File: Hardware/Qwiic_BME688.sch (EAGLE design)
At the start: 28 parts, among them J1 DNP, J2 QWIIC_RA, J4 QWIIC_RA, U1 BME688LGA

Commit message: Board routed
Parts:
- C1, C2: device SparkFun-Capacitors:0.1UF-0402-16V-10% -> SparkFun-Capacitors:0.1UF-0603-100V-10%
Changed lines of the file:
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@@
 <grid distance="0.1" unitdist="inch" unit="inch" style="lines" multiple="1" display="no" altdistance="0.01" altunitdist="inch" altunit="inch"/>
 <layers>
-<layer number="1" name="Top" color="4" fill="1" visible="no" active="no"/>
-<layer number="2" name="Route2" color="1" fill="3" visible="no" active="no"/>
-<layer number="3" name="Route3" color="4" fill="3" visible="no" active="no"/>
-<layer number="4" name="Route4" color="1" fill="4" visible="no" active="no"/>
-<layer number="5" name="Route5" color="4" fill="4" visible="no" active="no"/>
-<layer number="6" name="Route6" color="1" fill="8" visible="no" active="no"/>
-<layer number="7" name="Route7" color="4" fill="8" visible="no" active="no"/>
-<layer number="8" name="Route8" color="1" fill="2" visible="no" active="no"/>
-<layer number="9" name="Route9" color="4" fill="2" visible="no" active="no"/>
-<layer number="10" name="Route10" color="1" fill="7" visible="no" active="no"/>
-<layer number="11" name="Route11" color="4" fill="7" visible="no" active="no"/>
-<layer number="12" name="Route12" color="1" fill="5" visible="no" active="no"/>
-<layer number="13" name="Route13" color="4" fill="5" visible="no" active="no"/>
-<layer number="14" name="Route14" color="1" fill="6" visible="no" active="no"/>
-<layer number="15" name="Route15" color="4" fill="6" visible="no" active="no"/>
-<layer number="16" name="Bottom" color="1" fill="1" visible="no" active="no"/>
-<layer number="17" name="Pads" color="2" fill="1" visible="no" active="no"/>
-<layer number="18" name="Vias" color="2" fill="1" visible="no" active="no"/>
-<layer number="19" name="Unrouted" color="6" fill="1" visible="no" active="no"/>
-<layer number="20" name="Dimension" color="24" fill="1" visible="no" active="no"/>
-<layer number="21" name="tPlace" color="16" fill="1" visible="no" active="no"/>
-<layer number="22" name="bPlace" color="14" fill="1" visible="no" active="no"/>
-<layer number="23" name="tOrigins" color="15" fill="1" visible="no" active="no"/>
-<layer number="24" name="bOrigins" color="15" fill="1" visible="no" active="no"/>
-<layer number="25" name="tNames" color="7" fill="1" visible="no" active="no"/>
-<layer number="26" name="bNames" color="7" fill="1" visible="no" active="no"/>
-<layer number="27" name="tValues" color="7" fill="1" visible="no" active="no"/>
-<layer number="28" name="bValues" color="7" fill="1" visible="no" active="no"/>
+<layer number="1" name="Top" color="4" fill="1" visible="yes" active="no"/>
+<layer number="2" name="Route2" color="1" fill="3" visible="yes" active="no"/>
+<layer number="3" name="Route3" color="4" fill="3" visible="yes" active="no"/>
+<layer number="4" name="Route4" color="1" fill="4" visible="yes" active="no"/>
+<layer number="5" name="Route5" color="4" fill="4" visible="yes" active="no"/>
+<layer number="6" name="Route6" color="1" fill="8" visible="yes" active="no"/>
+<layer number="7" name="Route7" color="4" fill="8" visible="yes" active="no"/>
+<layer number="8" name="Route8" color="1" fill="2" visible="yes" active="no"/>
+<layer number="9" name="Route9" color="4" fill="2" visible="yes" active="no"/>
+<layer number="10" name="Route10" color="1" fill="7" visible="yes" active="no"/>
+<layer number="11" name="Route11" color="4" fill="7" visible="yes" active="no"/>
+<layer number="12" name="Route12" color="1" fill="5" visible="yes" active="no"/>
+<layer number="13" name="Route13" color="4" fill="5" visible="yes" active="no"/>
+<layer number="14" name="Route14" color="1" fill="6" visible="yes" active="no"/>
+<layer number="15" name="Route15" color="4" fill="6" visible="yes" active="no"/>
+<layer number="16" name="Bottom" color="1" fill="1" visible="yes" active="no"/>
+<layer number="17" name="Pads" color="2" fill="1" visible="yes" active="no"/>
+<layer number="18" name="Vias" color="2" fill="1" visible="yes" active="no"/>
+<layer number="19" name="Unrouted" color="6" fill="1" visible="yes" active="no"/>
+<layer number="20" name="Dimension" color="24" fill="1" visible="yes" active="no"/>
+<layer number="21" name="tPlace" color="16" fill="1" visible="yes" active="no"/>
+<layer number="22" name="bPlace" color="14" fill="1" visible="yes" active="no"/>
+<layer number="23" name="tOrigins" color="15" fill="1" visible="yes" active="no"/>
+<layer number="24" name="bOrigins" color="15" fill="1" visible="yes" active="no"/>
+<layer number="25" name="tNames" color="7" fill="1" visible="yes" active="no"/>
+<layer number="26" name="bNames" color="7" fill="1" visible="yes" active="no"/>
+<layer number="27" name="tValues" color="7" fill="1" visible="yes" active="no"/>
+<layer number="28" name="bValues" color="7" fill="1" visible="yes" active="no"/>
 <layer number="29" name="tStop" color="7" fill="3" visible="no" active="no"/>
 <layer number="30" name="bStop" color="7" fill="6" visible="no" active="no"/>
@@
 <layer number="35" name="tGlue" color="7" fill="4" visible="no" active="no"/>
 <layer number="36" name="bGlue" color="7" fill="5" visible="no" active="no"/>
-<layer number="37" name="tTest" color="7" fill="1" visible="no" active="no"/>
-<layer number="38" name="bTest" color="7" fill="1" visible="no" active="no"/>
+<layer number="37" name="tTest" color="7" fill="1" visible="yes" active="no"/>
+<layer number="38" name="bTest" color="7" fill="1" visible="yes" active="no"/>
 <layer number="39" name="tKeepout" color="4" fill="11" visible="no" active="no"/>
 <layer number="40" name="bKeepout" color="1" fill="11" visible="no" active="no"/>
@@
 <layer number="44" name="Drills" color="7" fill="1" visible="no" active="no"/>
 <layer number="45" name="Holes" color="7" fill="1" visible="no" active="no"/>
-<layer number="46" name="Milling" color="3" fill="1" visible="no" active="no"/>
-<layer number="47" name="Measures" color="7" fill="1" visible="no" active="no"/>
-<layer number="48" name="Document" color="7" fill="1" visible="no" active="no"/>
-<layer number="49" name="Reference" color="7" fill="1" visible="no" active="no"/>
-<layer number="50" name="dxf" color="7" fill="1" visible="no" active="no"/>
-<layer number="51" name="tDocu" color="6" fill="1" visible="no" active="no"/>
-<layer number="52" name="bDocu" color="7" fill="1" visible="no" active="no"/>
-<layer number="53" name="tGND_GNDA" color="7" fill="9" visible="no" active="no"/>
-<layer number="54" name="bGND_GNDA" color="1" fill="9" visible="no" active="no"/>
-<layer number="56" name="wert" color="7" fill="1" visible="no" active="no"/>
-<layer number="57" name="tCAD" color="7" fill="1" visible="no" active="no"/>
-<layer number="58" name="bCopper" color="7" fill="1" visible="no" active="no"/>
-<layer number="59" name="tCarbon" color="7" fill="1" visible="no" active="no"/>
-<layer number="60" name="bCarbon" color="7" fill="1" visible="no" active="no"/>
+<layer number="46" name="Milling" color="3" fill="1" visible="yes" active="no"/>
+<layer number="47" name="Measures" color="7" fill="1" visible="yes" active="no"/>
+<layer number="48" name="Document" color="7" fill="1" visible="yes" active="no"/>
+<layer number="49" name="Reference" color="7" fill="1" visible="yes" active="no"/>
+<layer number="50" name="dxf" color="7" fill="1" visible="yes" active="no"/>
+<layer number="51" name="tDocu" color="6" fill="1" visible="yes" active="no"/>
+<layer number="52" name="bDocu" color="7" fill="1" visible="yes" active="no"/>
+<layer number="53" name="tGND_GNDA" color="7" fill="9" visible="yes" active="no"/>
+<layer number="54" name="bGND_GNDA" color="1" fill="9" visible="yes" active="no"/>
+<layer number="56" name="wert" color="7" fill="1" visible="yes" active="no"/>
+<layer number="57" name="tCAD" color="7" fill="1" visible="yes" active="no"/>
+<layer number="58" name="bCopper" color="7" fill="1" visible="yes" active="no"/>
+<layer number="59" name="tCarbon" color="7" fill="1" visible="yes" active="no"/>
+<layer number="60" name="bCarbon" color="7" fill="1" visible="yes" active="no"/>
 <layer number="88" name="SimResults" color="9" fill="1" visible="no" active="yes"/>
 <layer number="89" name="SimProbes" color="9" fill="1" visible="no" active="yes"/>
@@
 <part name="GND2" library="SparkFun-PowerSymbols" deviceset="GND" device=""/>
 <part name="SUPPLY1" library="SparkFun-PowerSymbols" deviceset="3.3V" device=""/>
-<part name="C1" library="SparkFun-Capacitors" deviceset="0.1UF" device="-0402-16V-10%" value="0.1uF"/>
-<part name="C2" library="SparkFun-Capacitors" deviceset="0.1UF" device="-0402-16V-10%" value="0.1uF"/>
+<part name="C1" library="SparkFun-Capacitors" deviceset="0.1UF" device="-0603-100V-10%" value="0.1uF"/>
+<part name="C2" library="SparkFun-Capacitors" deviceset="0.1UF" device="-0603-100V-10%" value="0.1uF"/>
 <part name="SUPPLY2" library="SparkFun-PowerSymbols" deviceset="3.3V" device=""/>
 <part name="SUPPLY3" library="SparkFun-PowerSymbols" deviceset="3.3V" device=""/>

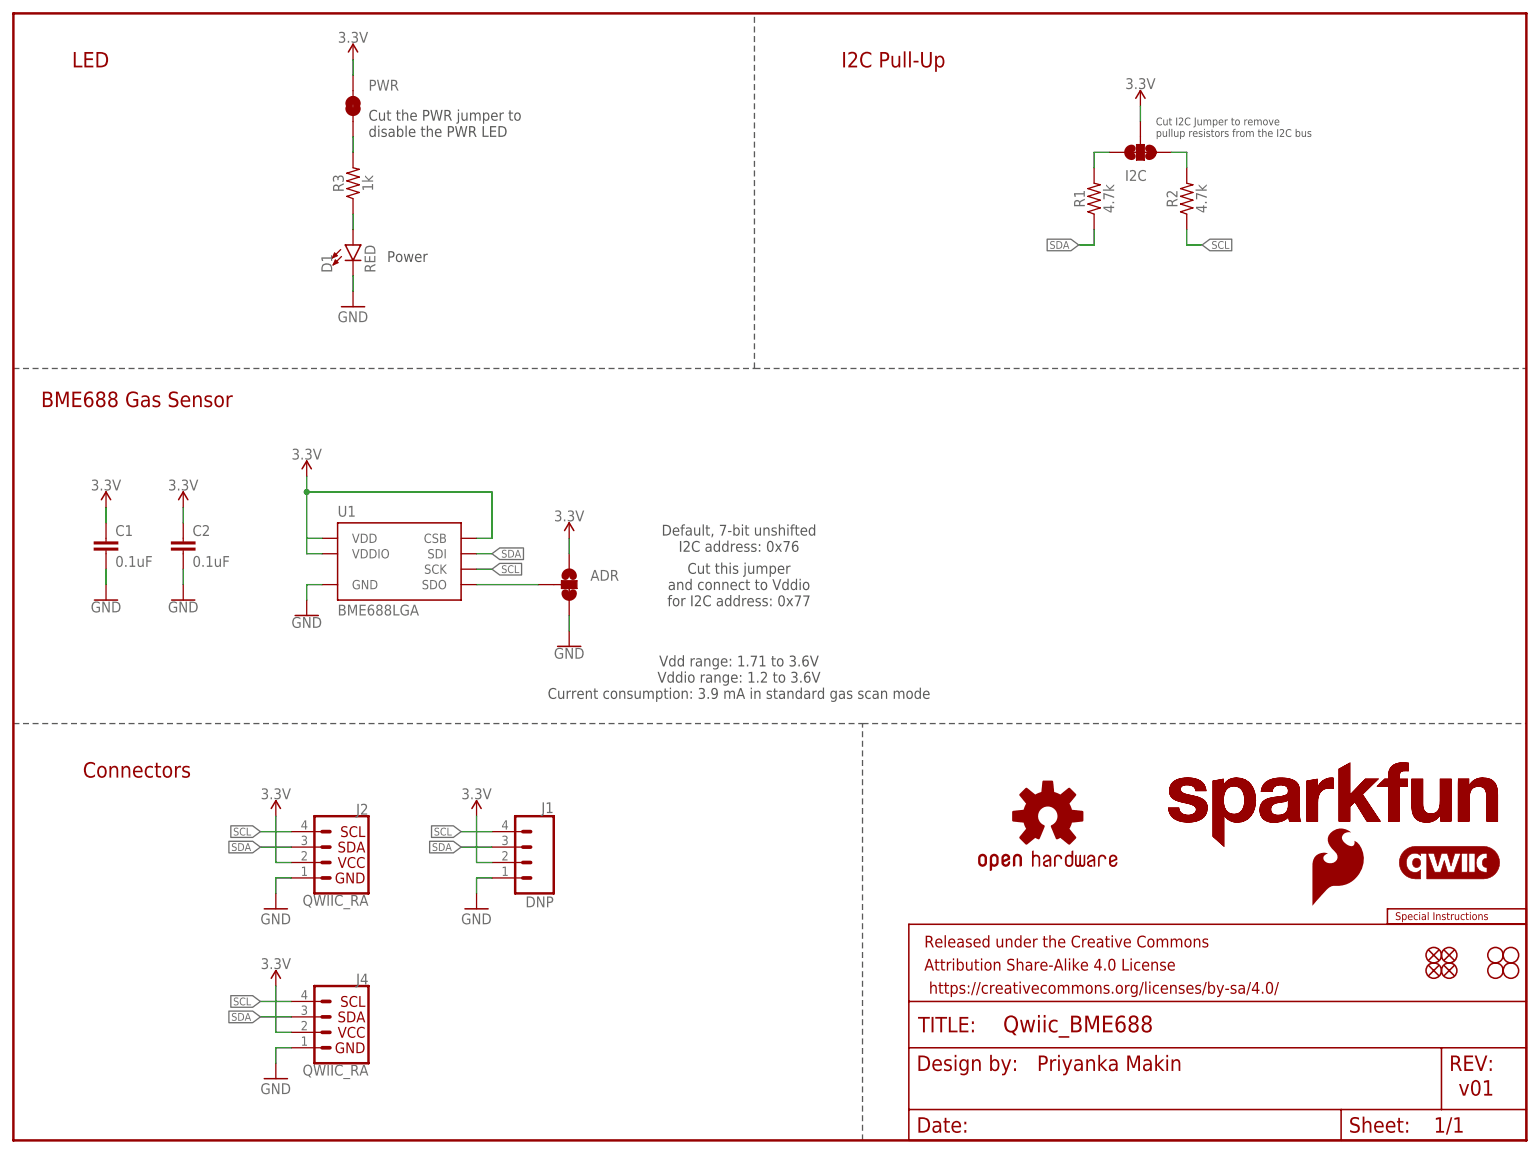
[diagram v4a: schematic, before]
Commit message: Design review updates
Schematic:
* Add headers for CSB and SDO
* Add NC jumper between CSB and 3.3V
* Add 10k resistor for 3-way jumper
* Replace I2C pullups with 2.2kohms
* Increase the size of fiducials
Board:
* Change version number to v01
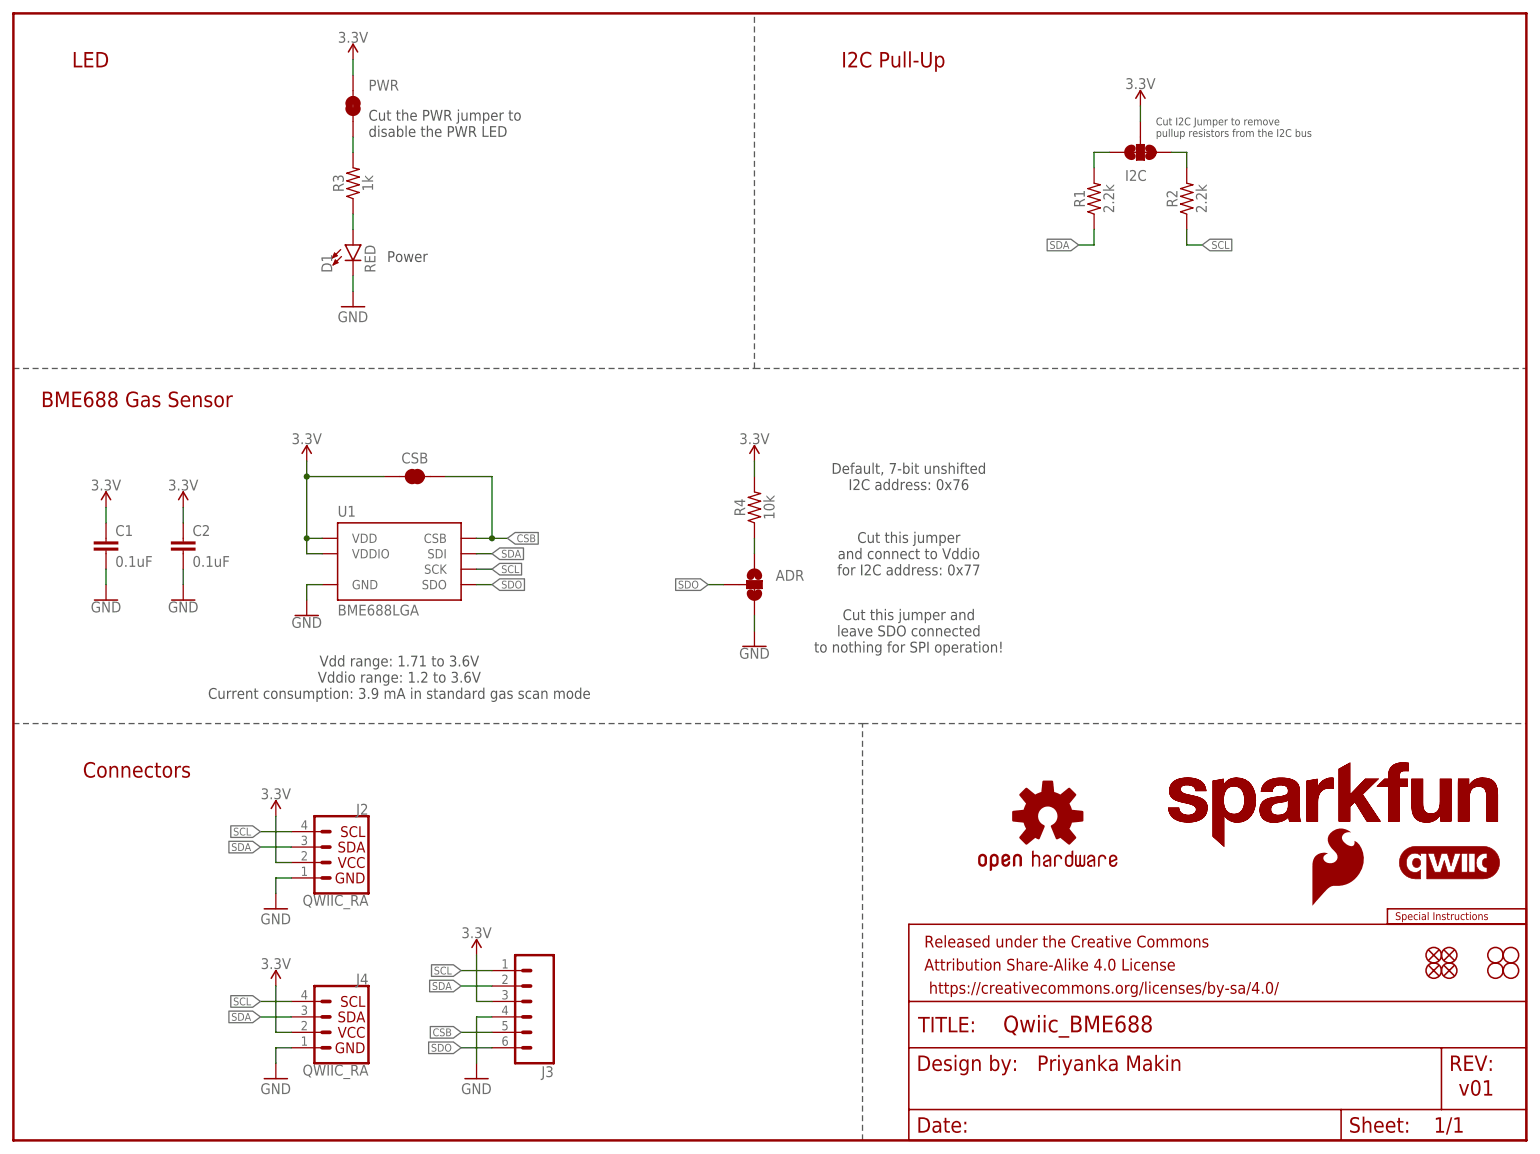
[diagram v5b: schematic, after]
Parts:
- removed J1: DNP, SparkFun-Connectors:CONN_041X04_NO_SILK
- added CSB: JUMPER-SMT_2_NC_TRACE_SILK, SparkFun-Jumpers:JUMPER-SMT_2_NC_TRACE_SILK
- added J3: (no value), SparkFun-Connectors:CONN_06NO_SILK_NO_POP
- added R4: 10k, SparkFun-Resistors:10KOHM-0603-1/10W-1%
- JP1, JP2, JP5, JP6: value FIDUCIAL0.2MM -> FIDUCIALUFIDUCIAL; device SparkFun-Aesthetics:FIDUCIAL0.2MM -> SparkFun-Aesthetics:FIDUCIALUFIDUCIAL
- R1, R2: value 4.7k -> 2.2k; device SparkFun-Resistors:4.7KOHM-0603-1/10W-1% -> SparkFun-Resistors:2.2KOHM-0603-1/10W-1%
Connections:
- removed net N$6: ADR.2, U1.SDO
- new net CSB: CSB.2, J3.5, U1.CSB
- new net N$5: ADR.1, R4.1
- new net SDO: ADR.2, J3.6, U1.SDO
- net 3.3V: now also CSB.1, J3.3, R4.2; no longer ADR.1, J1.2, U1.CSB
- net GND: now also J3.4; no longer J1.1
- net SCL: now also J3.1; no longer J1.4
- net SDA: now also J3.2; no longer J1.3
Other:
- note added: "Cut this jumper and leave SDO connected to nothing for SPI operation!"
- moved on the sheet: ADR

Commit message: Engineering checklist
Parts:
- renumbered PWR to LED
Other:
- note added: "Cut the CSB jumper if you want to use this pin as CS in SPI mode."
- note added: "Cut the LED jumper to disable the PWR LED"
- note removed: "Cut the PWR jumper to disable the PWR LED"
